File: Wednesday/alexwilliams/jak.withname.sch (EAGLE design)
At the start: 23 parts, among them U1_0_BRAIN ADAFRUIT-PRO-TRINKET-5V-BOB, U1_12_CASTER_2 CASTERADAFRUIT-3/4IN, U1_2_DISPLAY ADAFRUIT-1.2IN-8X8-LED-BACKPA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, U1_3_BUZZER BUZZERPTH, U1_6_CASTER CASTERADAFRUIT-3/4IN

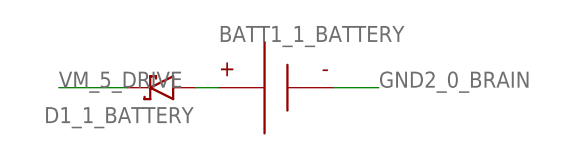
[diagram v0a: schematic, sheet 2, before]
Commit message: Expanded drills because we have run out of 0.8mm
git-svn-id: svn+ssh://bbfs-01.calit2.net/grw/Gordon/svn/trunk/Gadgets/Designs/CSE91Robots@22863 2cf53259-273a-af40-bda6-69d31023b8ec
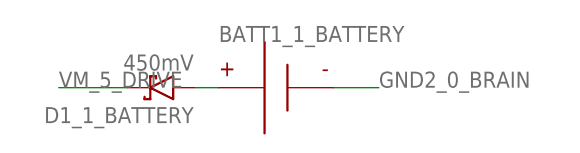
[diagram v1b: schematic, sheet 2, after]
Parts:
- D1_1_BATTERY: value (none) -> 450mV
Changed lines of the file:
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@@
 <layer number="10" name="Route10" color="1" fill="7" visible="no" active="no"/>
 <layer number="11" name="Route11" color="4" fill="7" visible="no" active="no"/>
+<layer number="12" name="Route12" color="1" fill="5" visible="no" active="no"/>
 <layer number="13" name="Route13" color="4" fill="5" visible="no" active="no"/>
 <layer number="14" name="Route14" color="1" fill="6" visible="no" active="no"/>
@@
 <layer number="48" name="Document" color="7" fill="1" visible="no" active="no"/>
 <layer number="49" name="Reference" color="7" fill="1" visible="no" active="no"/>
+<layer number="50" name="dxf" color="7" fill="1" visible="no" active="no"/>
 <layer number="51" name="tDocu" color="7" fill="1" visible="no" active="no"/>
 <layer number="52" name="bDocu" color="7" fill="1" visible="no" active="no"/>
+<layer number="53" name="tGND_GNDA" color="7" fill="9" visible="no" active="no"/>
+<layer number="54" name="bGND_GNDA" color="1" fill="9" visible="no" active="no"/>
+<layer number="56" name="wert" color="7" fill="1" visible="no" active="no"/>
+<layer number="57" name="tCAD" color="7" fill="1" visible="no" active="no"/>
 <layer number="90" name="Modules" color="5" fill="1" visible="yes" active="yes"/>
 <layer number="91" name="Nets" color="2" fill="1" visible="yes" active="yes"/>
@@
 <layer number="97" name="Info" color="7" fill="1" visible="yes" active="yes"/>
 <layer number="98" name="Guide" color="6" fill="1" visible="yes" active="yes"/>
+<layer number="99" name="SpiceOrder" color="7" fill="1" visible="no" active="no"/>
 <layer number="100" name="tFaceplateCover" color="11" fill="1" visible="yes" active="yes"/>
 <layer number="101" name="bFaceplateCover" color="11" fill="1" visible="yes" active="yes"/>
+<layer number="102" name="Vscore" color="7" fill="1" visible="no" active="no"/>
+<layer number="103" name="fp3" color="7" fill="1" visible="no" active="no"/>
+<layer number="104" name="Name" color="7" fill="1" visible="no" active="no"/>
+<layer number="105" name="Beschreib" color="9" fill="1" visible="no" active="no"/>
+<layer number="106" name="BGA-Top" color="4" fill="1" visible="no" active="no"/>
+<layer number="107" name="BD-Top" color="5" fill="1" visible="no" active="no"/>
+<layer number="108" name="fp8" color="7" fill="1" visible="no" active="no"/>
+<layer number="109" name="fp9" color="7" fill="1" visible="no" active="no"/>
+<layer number="110" name="fp0" color="7" fill="1" visible="no" active="no"/>
+<layer number="111" name="LPC17xx" color="7" fill="1" visible="no" active="no"/>
+<layer number="112" name="tSilk" color="7" fill="1" visible="no" active="no"/>
+<layer number="113" name="IDFDebug" color="4" fill="1" visible="yes" active="yes"/>
 <layer number="114" name="Unresolved" color="12" fill="1" visible="yes" active="yes"/>
 <layer number="115" name="Resolved" color="10" fill="1" visible="yes" active="yes"/>
 <layer number="116" name="Generic" color="9" fill="1" visible="yes" active="yes"/>
+<layer number="118" name="Rect_Pads" color="7" fill="1" visible="yes" active="yes"/>
+<layer number="121" name="_tsilk" color="7" fill="1" visible="no" active="no"/>
+<layer number="122" name="_bsilk" color="7" fill="1" visible="no" active="no"/>
+<layer number="123" name="tTestmark" color="7" fill="1" visible="no" active="no"/>
+<layer number="124" name="bTestmark" color="7" fill="1" visible="no" active="no"/>
+<layer number="125" name="_tNames" color="7" fill="1" visible="no" active="no"/>
+<layer number="126" name="_bNames" color="7" fill="1" visible="no" active="no"/>
+<layer number="127" name="_tValues" color="7" fill="1" visible="no" active="no"/>
+<layer number="128" name="_bValues" color="7" fill="1" visible="no" active="no"/>
+<layer number="131" name="tAdjust" color="7" fill="1" visible="no" active="no"/>
+<layer number="132" name="bAdjust" color="7" fill="1" visible="no" active="no"/>
+<layer number="144" name="Drill_legend" color="7" fill="1" visible="no" active="no"/>
 <layer number="150" name="tFaceplate" color="11" fill="1" visible="yes" active="yes"/>
 <layer number="151" name="bFaceplate" color="11" fill="1" visible="yes" active="yes"/>
+<layer number="152" name="_bDocu" color="7" fill="1" visible="no" active="no"/>
+<layer number="153" name="FabDoc1" color="6" fill="1" visible="no" active="no"/>
+<layer number="154" name="FabDoc2" color="2" fill="1" visible="no" active="no"/>
+<layer number="155" name="FabDoc3" color="7" fill="15" visible="no" active="no"/>
 <layer number="160" name="tMountFaceplate" color="11" fill="1" visible="no" active="yes"/>
 <layer number="161" name="bMountFaceplate" color="11" fill="1" visible="no" active="yes"/>
@@
 <layer number="167" name="Fiducials" color="13" fill="1" visible="yes" active="yes"/>
 <layer number="169" name="internal" color="15" fill="1" visible="yes" active="yes"/>
+<layer number="199" name="Contour" color="7" fill="1" visible="no" active="no"/>
+<layer number="200" name="200bmp" color="1" fill="10" visible="no" active="no"/>
+<layer number="201" name="201bmp" color="2" fill="1" visible="no" active="no"/>
+<layer number="202" name="202bmp" color="3" fill="1" visible="no" active="no"/>
+<layer number="203" name="203bmp" color="4" fill="10" visible="no" active="no"/>
+<layer number="204" name="204bmp" color="5" fill="10" visible="no" active="no"/>
+<layer number="205" name="205bmp" color="6" fill="10" visible="no" active="no"/>
+<layer number="206" name="206bmp" color="7" fill="10" visible="no" active="no"/>
+<layer number="207" name="207bmp" color="8" fill="10" visible="no" active="no"/>
+<layer number="208" name="208bmp" color="9" fill="10" visible="no" active="no"/>
+<layer number="209" name="209bmp" color="7" fill="1" visible="no" active="no"/>
+<layer number="210" name="210bmp" color="7" fill="1" visible="no" active="no"/>
+<layer number="211" name="211bmp" color="7" fill="1" visible="no" active="no"/>
+<layer number="212" name="212bmp" color="7" fill="1" visible="no" active="no"/>
+<layer number="213" name="213bmp" color="7" fill="1" visible="no" active="no"/>
+<layer number="214" name="214bmp" color="7" fill="1" visible="no" active="no"/>
+<layer number="215" name="215bmp" color="7" fill="1" visible="no" active="no"/>
+<layer number="216" name="216bmp" color="7" fill="1" visible="no" active="no"/>
+<layer number="217" name="217bmp" color="18" fill="1" visible="no" active="no"/>
+<layer number="218" name="218bmp" color="19" fill="1" visible="no" active="no"/>
+<layer number="219" name="219bmp" color="20" fill="1" visible="no" active="no"/>
+<layer number="220" name="220bmp" color="21" fill="1" visible="no" active="no"/>
+<layer number="221" name="221bmp" color="22" fill="1" visible="no" active="no"/>
+<layer number="222" name="222bmp" color="23" fill="1" visible="no" active="no"/>
+<layer number="223" name="223bmp" color="24" fill="1" visible="no" active="no"/>
+<layer number="224" name="224bmp" color="25" fill="1" visible="no" active="no"/>
+<layer number="231" name="Eagle3D_PG1" color="7" fill="1" visible="yes" active="yes"/>
+<layer number="232" name="Eagle3D_PG2" color="7" fill="1" visible="yes" active="yes"/>
+<layer number="233" name="Eagle3D_PG3" color="7" fill="1" visible="yes" active="yes"/>
+<layer number="248" name="Housing" color="7" fill="1" visible="no" active="no"/>
+<layer number="249" name="Edge" color="7" fill="1" visible="no" active="no"/>
+<layer number="250" name="Descript" color="7" fill="1" visible="no" active="no"/>
+<layer number="251" name="SMDround" color="7" fill="1" visible="no" active="no"/>
+<layer number="254" name="cooling" color="7" fill="1" visible="no" active="no"/>
 </layers>
 <schematic xreflabel="%F%N/%S.%C%R" xrefpart="/%S.%C%R">
@@
 <part name="B1_9_BUTTON" library="Components" deviceset="BUTTON-TACTILE" device="-SQUARE" value="BUTTON-TACTILE-SQUARE"/>
 <part name="BATT1_1_BATTERY" library="Components" deviceset="BATTERY" device="-9V-VERTICAL"/>
-<part name="D1_1_BATTERY" library="KoalaBuild" deviceset="RESOLVED-DIODE-SCHOTTKY_" device="TH-DO-41-AND-DO-204AL">
+<part name="D1_1_BATTERY" library="KoalaBuild" deviceset="RESOLVED-DIODE-SCHOTTKY_" device="TH-DO-41-AND-DO-204AL" value="450mV">
 <attribute name="DATASHEET" value="http://www.st.com/web/en/resource/technical/document/datasheet/CD00001625.pdf"/>
 <attribute name="DB" value="/Users/sciencectn/Documents/nvsl/Gadgets/Tools/Koala/Koala/PartLibrary/Digikey/Schottky-Diodes-TH.csv"/>
@@
 <attribute name="VALUE_QUERY" value="150"/>
 </part>
-<part name="U1_0_BRAIN" library="BOBs" deviceset="ADAFRUIT-PRO-TRINKET-5V" device="-BOB" value=""/>
-<part name="U1_12_CASTER_2" library="Components" deviceset="CASTER" device="ADAFRUIT-3/4IN" value=""/>
-<part name="U1_2_DISPLAY" library="BOBs" deviceset="ADAFRUIT-1.2IN-8X8-LED-BACKPACK" device="-BOB" value=""/>
-<part name="U1_3_BUZZER" library="Components" deviceset="BUZZER" device="PTH" value=""/>
-<part name="U1_6_CASTER" library="Components" deviceset="CASTER" device="ADAFRUIT-3/4IN" value=""/>
+<part name="U1_0_BRAIN" library="BOBs" deviceset="ADAFRUIT-PRO-TRINKET-5V" device="-BOB" value="ADAFRUIT-PRO-TRINKET-5V-BOB"/>
+<part name="U1_12_CASTER_2" library="Components" deviceset="CASTER" device="ADAFRUIT-3/4IN" value="CASTERADAFRUIT-3/4IN"/>
+<part name="U1_2_DISPLAY" library="BOBs" deviceset="ADAFRUIT-1.2IN-8X8-LED-BACKPACK" device="-BOB" value="ADAFRUIT-1.2IN-8X8-LED-BACKPACK-BOB"/>
+<part name="U1_3_BUZZER" library="Components" deviceset="BUZZER" device="PTH" value="BUZZERPTH"/>
+<part name="U1_6_CASTER" library="Components" deviceset="CASTER" device="ADAFRUIT-3/4IN" value="CASTERADAFRUIT-3/4IN"/>
 </parts>
 <sheets>
